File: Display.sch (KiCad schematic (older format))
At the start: 6 parts

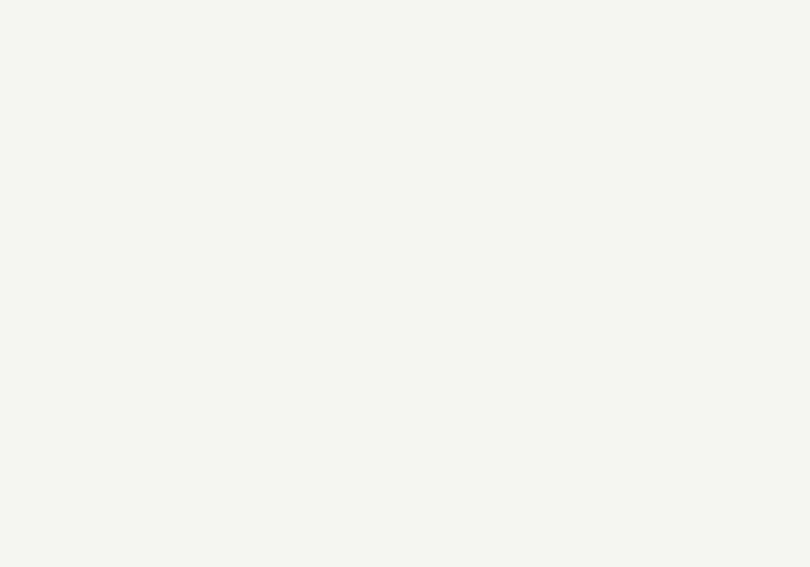
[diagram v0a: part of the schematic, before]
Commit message: Resolved an issue with the field names of resistors on anode and grid driver sheets
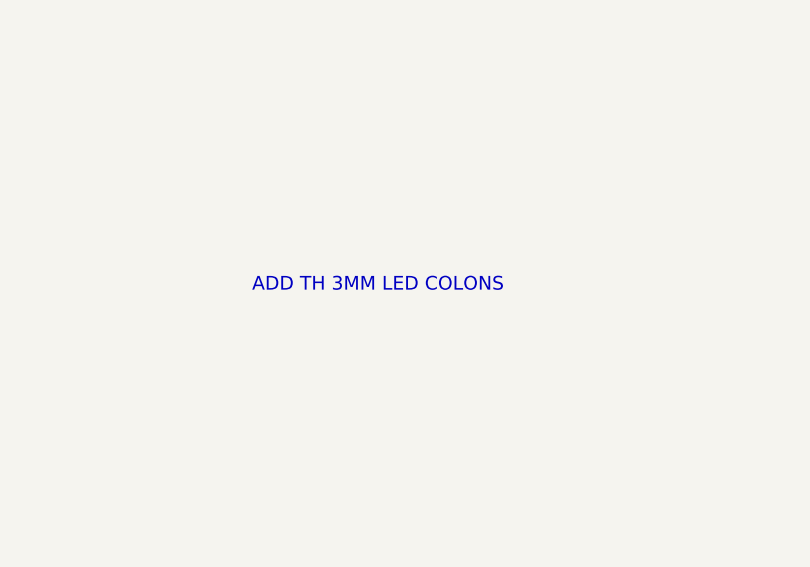
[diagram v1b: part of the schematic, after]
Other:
- note added: "ADD TH 3MM LED COLONS"
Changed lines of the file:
@@
 Text GLabel 4020 5780 3    60   UnSpc ~ 0
 Grid_0
+Text Notes 7350 4880 0    60   ~ 0
+ADD TH 3MM LED COLONS
 $EndSCHEMATC

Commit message: Added colons and drivers to display sheet
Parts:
- added C? (x2): 0.1uF, Capacitors_SMD:C_0603, symbol Custom-Library:C_Custom
- added D? (x2): Green, LEDs:LED_D3.0mm_Horizontal_O1.27mm_Z10.0mm, symbol Custom-Library:LED_ALT_Custom
- added D? (x2): Green, LEDs:LED_D3.0mm_Horizontal_O1.27mm_Z2.0mm, symbol Custom-Library:LED_ALT_Custom
- added R? (x4): 1k, Resistors_SMD:R_0603, symbol VFD_Clock-rescue:Res_Custom
- added R? (x4): 10k, Resistors_SMD:R_0603, symbol VFD_Clock-rescue:Res_Custom
- added U? (x2): 74LVC1G38, TO_SOT_Packages_SMD:SOT-23-5, symbol Custom-Library:74LVC1G38_Custom
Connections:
- net labels added: +3.3V, Colon_1, Colon_2, DIM_PWM
- wire segments 0 -> 20
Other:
- note removed: "ADD TH 3MM LED COLONS"

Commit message: Annotated all components, finished assigning footprints, netlist generated
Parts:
- U1901, U1902: renamed from U?; footprint TO_SOT_Packages_SMD:SOT-23-5 -> TO_SOT_Packages_SMD:SOT-353_SC-70-5; Digi-Key PN (none) -> 296-17907-1-ND
- gave numbers to parts that had none: 14

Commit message: Slight netlist modifications, pulled changes into  PCB
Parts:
- D1901, D1903: footprint LEDs:LED_D3.0mm_Horizontal_O1.27mm_Z10.0mm -> LEDs:LED_D3.0mm_Horizontal_O3.81mm_Z10.0mm
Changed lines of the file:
@@
 F 0 "D1901" H 6710 4020 50  0000 C CNN
 F 1 "Green" H 6710 3820 50  0000 C CNN
-F 2 "LEDs:LED_D3.0mm_Horizontal_O1.27mm_Z10.0mm" H 6710 3920 50  0001 C CNN
+F 2 "LEDs:LED_D3.0mm_Horizontal_O3.81mm_Z10.0mm" H 6710 3920 50  0001 C CNN
 F 3 "" H 6710 3920 50  0001 C CNN
 F 4 "TH" H 6710 3720 50  0000 C CNN "display_footprint"
@@
 F 0 "D1903" H 8240 4020 50  0000 C CNN
 F 1 "Green" H 8240 3820 50  0000 C CNN
-F 2 "LEDs:LED_D3.0mm_Horizontal_O1.27mm_Z10.0mm" H 8240 3920 50  0001 C CNN
+F 2 "LEDs:LED_D3.0mm_Horizontal_O3.81mm_Z10.0mm" H 8240 3920 50  0001 C CNN
 F 3 "" H 8240 3920 50  0001 C CNN
 F 4 "TH" H 8240 3720 50  0000 C CNN "display_footprint"

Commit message: Added a bunch of Digi-Key PN's
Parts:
- C1901, C1902: Digi-Key PN (none) -> 399-6856-1-ND
- D1901, D1902, D1903, D1904: Digi-Key PN PN -> 732-11401-ND
- R1901, R1902, R1907, R1908: Digi-Key PN (none) -> 541-10.0KHCT-ND
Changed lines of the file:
@@
 F 5 "1%" H 6780 4200 50  0000 L CNN "Tolerance"
 F 6 "1/10W" H 6770 4270 50  0000 L CNN "Wattage"
+F 7 "" H 0   0   50  0001 C CNN "Digi-Key PN"
 	1    6710 4220
 	-1   0    0    -1
@@
 F 3 "" H 6710 3920 50  0001 C CNN
 F 4 "TH" H 6710 3720 50  0000 C CNN "display_footprint"
-F 5 "PN" H 6910 4220 60  0001 C CNN "Digi-Key PN"
+F 5 "	732-11401-ND" H 6910 4220 60  0001 C CNN "Digi-Key PN"
 	1    6710 3920
 	0    -1   -1   0
@@
 F 5 "1%" H 7390 4200 50  0000 L CNN "Tolerance"
 F 6 "1/10W" H 7380 4270 50  0000 L CNN "Wattage"
+F 7 "" H 0   0   50  0001 C CNN "Digi-Key PN"
 	1    7320 4220
 	-1   0    0    -1
@@
 F 3 "" H 7320 3920 50  0001 C CNN
 F 4 "TH" H 7320 3720 50  0000 C CNN "display_footprint"
-F 5 "PN" H 7520 4220 60  0001 C CNN "Digi-Key PN"
+F 5 "	732-11401-ND" H 7520 4220 60  0001 C CNN "Digi-Key PN"
 	1    7320 3920
 	0    -1   -1   0
@@
 F 5 "1%" H 8310 4200 50  0000 L CNN "Tolerance"
 F 6 "1/10W" H 8300 4270 50  0000 L CNN "Wattage"
+F 7 "" H 0   0   50  0001 C CNN "Digi-Key PN"
 	1    8240 4220
 	-1   0    0    -1
@@
 F 3 "" H 8240 3920 50  0001 C CNN
 F 4 "TH" H 8240 3720 50  0000 C CNN "display_footprint"
-F 5 "PN" H 8440 4220 60  0001 C CNN "Digi-Key PN"
+F 5 "	732-11401-ND" H 8440 4220 60  0001 C CNN "Digi-Key PN"
 	1    8240 3920
 	0    -1   -1   0
@@
 F 5 "1%" H 8920 4200 50  0000 L CNN "Tolerance"
 F 6 "1/10W" H 8910 4270 50  0000 L CNN "Wattage"
+F 7 "" H 0   0   50  0001 C CNN "Digi-Key PN"
 	1    8850 4220
 	-1   0    0    -1
@@
 F 3 "" H 8850 3920 50  0001 C CNN
 F 4 "TH" H 8850 3720 50  0000 C CNN "display_footprint"
-F 5 "PN" H 9050 4220 60  0001 C CNN "Digi-Key PN"
+F 5 "	732-11401-ND" H 9050 4220 60  0001 C CNN "Digi-Key PN"
 	1    8850 3920
 	0    -1   -1   0
@@
 F 5 "1%" H 5980 5060 50  0001 L CNN "Tolerance"
 F 6 "1/10W" H 5970 5130 50  0001 L CNN "Wattage"
+F 7 "541-10.0KHCT-ND" H 0   0   50  0001 C CNN "Digi-Key PN"
 	1    5910 5080
 	-1   0    0    -1
@@
 F 5 "50V" H 6230 5510 50  0000 R CNN "Voltage"
 F 6 "X7R" H 6230 5410 50  0000 R CNN "Dielectric"
+F 7 "399-6856-1-ND" H 0   0   50  0001 C CNN "Digi-Key PN"
 	1    6380 5510
 	1    0    0    -1
@@
 F 5 "50V" H 9040 5510 50  0000 R CNN "Voltage"
 F 6 "X7R" H 9040 5410 50  0000 R CNN "Dielectric"
+F 7 "399-6856-1-ND" H 0   0   50  0001 C CNN "Digi-Key PN"
 	1    9190 5510
 	-1   0    0    -1
@@
 F 5 "1%" H 5760 5060 50  0001 L CNN "Tolerance"
 F 6 "1/10W" H 5750 5130 50  0001 L CNN "Wattage"
+F 7 "541-10.0KHCT-ND" H 0   0   50  0001 C CNN "Digi-Key PN"
 	1    5690 5080
 	-1   0    0    -1
@@
 F 5 "1%" H 9950 5060 50  0001 L CNN "Tolerance"
 F 6 "1/10W" H 9940 5130 50  0001 L CNN "Wattage"
+F 7 "541-10.0KHCT-ND" H 0   0   50  0001 C CNN "Digi-Key PN"
 	1    9880 5080
 	-1   0    0    -1
@@
 F 5 "1%" H 9730 5060 50  0001 L CNN "Tolerance"
 F 6 "1/10W" H 9720 5130 50  0001 L CNN "Wattage"
+F 7 "541-10.0KHCT-ND" H 0   0   50  0001 C CNN "Digi-Key PN"
 	1    9660 5080
 	-1   0    0    -1

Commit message: Arranged more components on PCB, cleaned up schematic, added page titles, finished finding DigiKey PN's
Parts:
- R1901, R1902, R1907, R1908: Digi-Key PN 541-10.0KHCT-ND -> P10.0KHCT-ND
- R1903, R1904, R1905, R1906: Digi-Key PN (none) -> RMCF0603FT1K00CT-ND
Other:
- note added: "VFD Tubes/Colons"
